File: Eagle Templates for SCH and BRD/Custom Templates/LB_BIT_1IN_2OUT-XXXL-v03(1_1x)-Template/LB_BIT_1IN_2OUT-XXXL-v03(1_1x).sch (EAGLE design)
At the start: 20 parts, among them U1 LV321SOT23-5, U2 LV321SOT23-5, U3 LV321SOT23-5

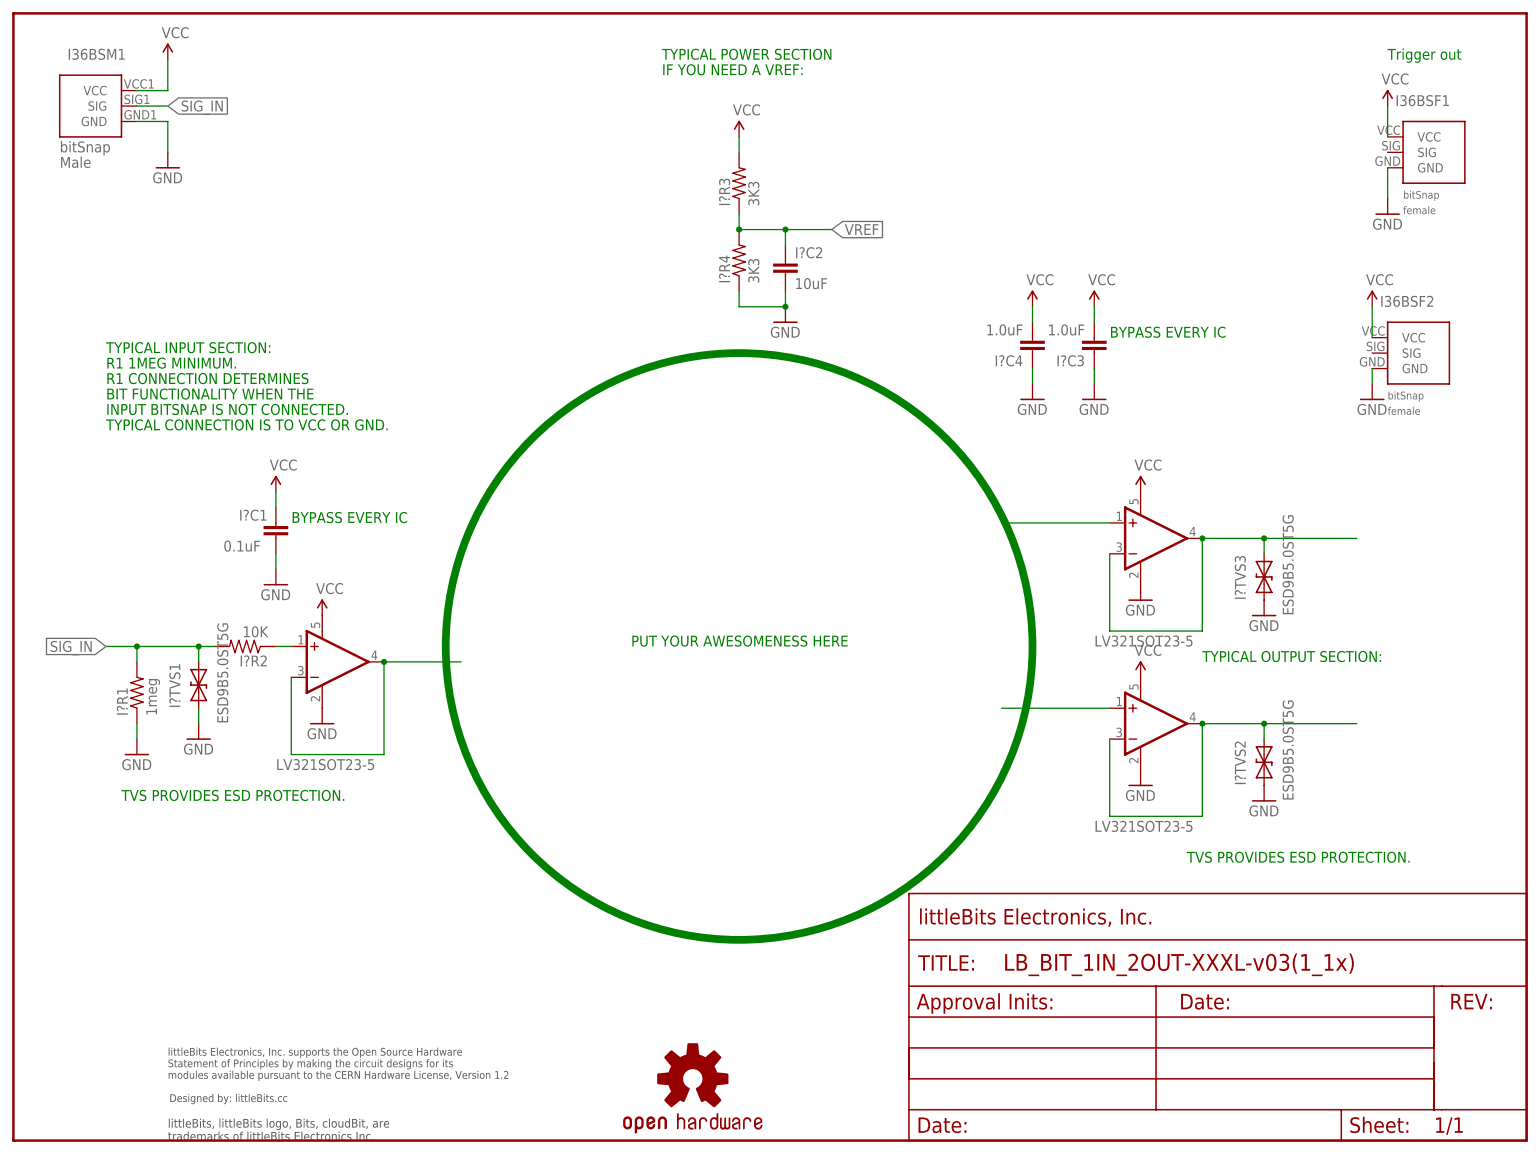
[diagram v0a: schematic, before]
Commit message: Updated templates
- Added ferrite beads
- Moved text and annotations off of Nets layer
- Minor layout changes
- Removed I/O/W prefix from reference designators
- Removed output stage components from output bits
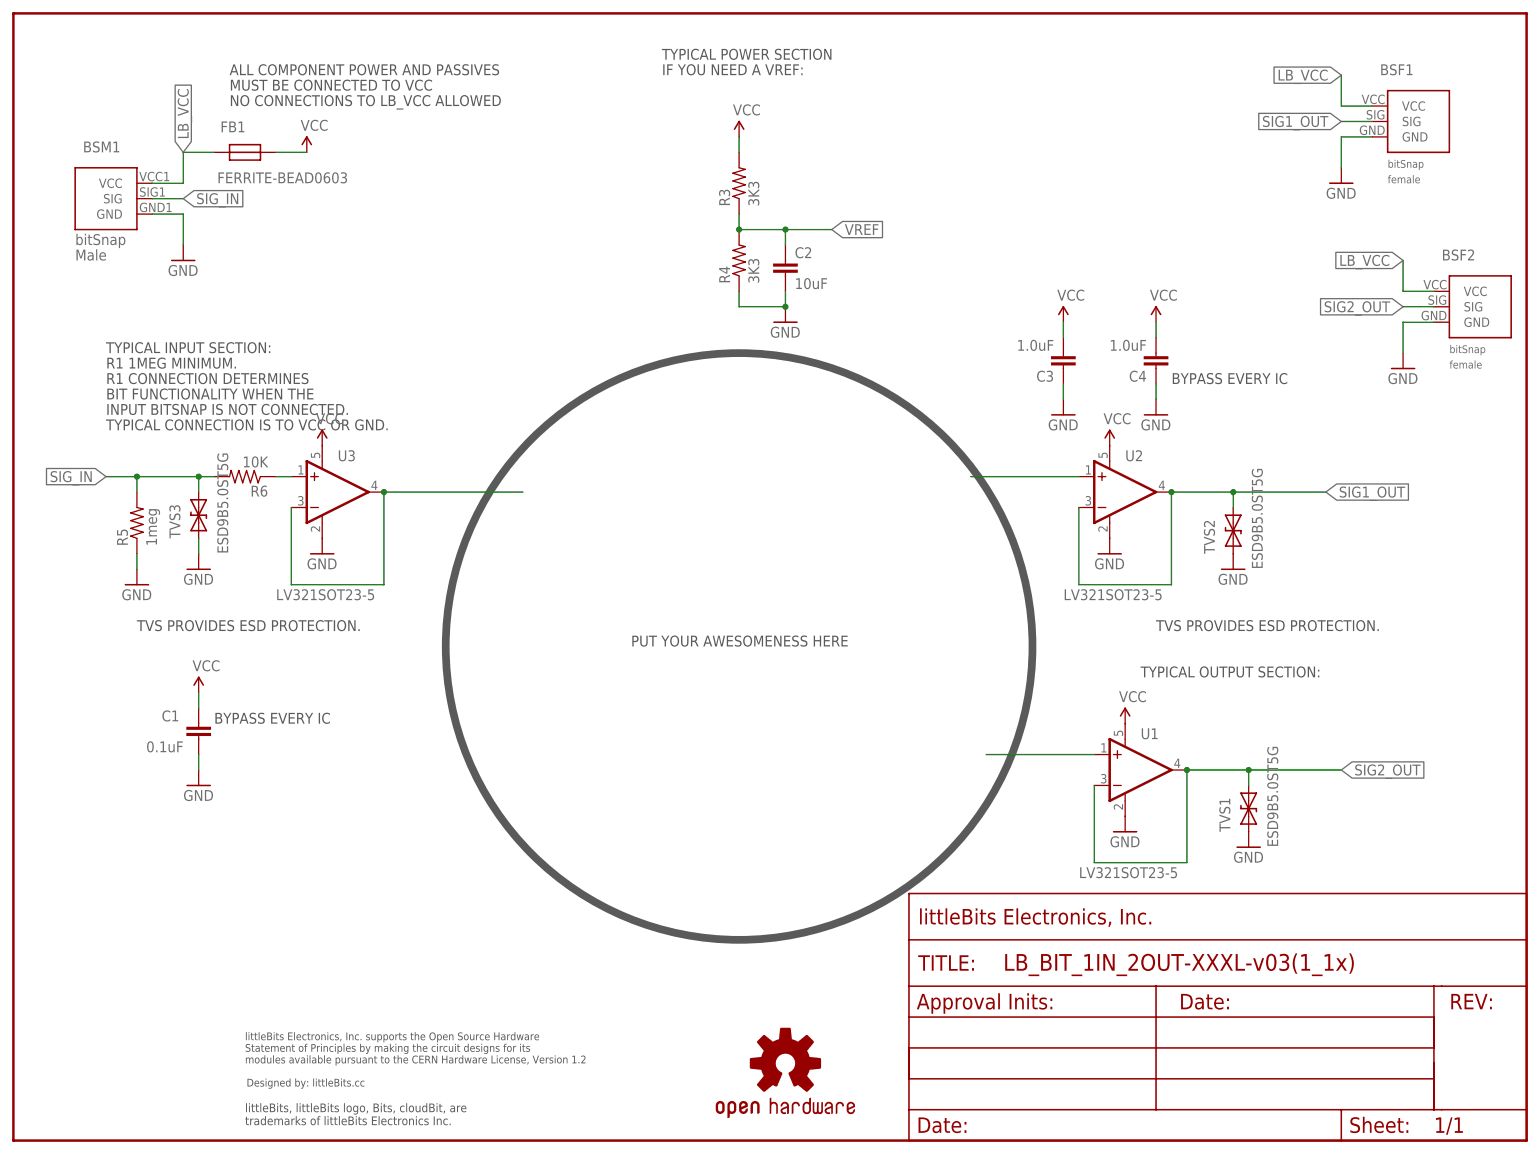
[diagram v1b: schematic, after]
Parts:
- removed I36BSF1, I36BSF2: BITSNAP_V03_FEMALE, bitSnap:BITSNAP_V03_FEMALE
- removed I36BSM1: BITSNAP_V03_MALE, bitSnap:BITSNAP_V03_MALE
- removed I?C1: 0.1uF, LITTLEBITS:CAPCAP-0603
- removed I?C3, I?C4: 1.0uF, LITTLEBITS:CAPCAP-0603
- removed I?R1: 1meg, LITTLEBITS:RESISTOR0603
- removed I?R2: 10K, LITTLEBITS:RESISTOR0603
- removed I?TVS1, I?TVS2, I?TVS3: ESD9B5.0ST5G, LITTLEBITS:DIODE-TVSSOD-923
- removed U$3: OSHWCREDIT, LITTLEBITS:OSHWCREDIT
- added BSF1, BSF2: BITSNAP_V03_FEMALE, bitSnap:BITSNAP_V03_FEMALE
- added BSM1: BITSNAP_V03_MALE, bitSnap:BITSNAP_V03_MALE
- added C1: 0.1uF, LITTLEBITS:CAPCAP-0603
- added C3, C4: 1.0uF, LITTLEBITS:CAPCAP-0603
- added FB1: FERRITE-BEAD0603, LITTLEBITS:FERRITE-BEAD0603
- added R5: 1meg, LITTLEBITS:RESISTOR0603
- added R6: 10K, LITTLEBITS:RESISTOR0603
- added TVS1, TVS2, TVS3: ESD9B5.0ST5G, LITTLEBITS:DIODE-TVSSOD-923
- added U$2: OSHWCREDIT, LITTLEBITS:OSHWCREDIT
- renumbered I?C2 to C2, I?R3 to R3, I?R4 to R4
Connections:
- removed net N$4: I?R2.1, U1.+IN
- removed net SIG_OUT: I?TVS2.C, U2.-IN, U2.OUT
- removed net SIG_OUT1: I?TVS3.C, U3.-IN, U3.OUT
- new net LB_VCC: BSF1.VCC, BSF2.VCC, BSM1.VCC, FB1.P$2
- new net N$5: R6.1, U3.+IN
- new net SIG1_OUT: BSF1.SIG, TVS2.C, U2.-IN, U2.OUT
- new net SIG2_OUT: BSF2.SIG, TVS1.C, U1.-IN, U1.OUT
- net GND: now also BSF1.GND, BSF2.GND, BSM1.GND, C1.2, C3.1, C4.1, R5.1, TVS1.A, TVS2.A, TVS3.A; no longer I36BSF1.GND, I36BSF2.GND, I36BSM1.GND, I?C1.2, I?C3.1, I?C4.1, I?R1.1, I?TVS1.A, I?TVS2.A, I?TVS3.A
- net N$1: now also U3.-IN, U3.OUT; no longer U3.+IN
- net N$2: now also U1.+IN; no longer U1.-IN, U1.OUT
- net SIG_IN: now also BSM1.SIG, R5.2, R6.2, TVS3.C; no longer I36BSM1.SIG, I?R1.2, I?R2.2, I?TVS1.C
- net VCC: now also C1.1, C3.2, C4.2, FB1.P$1; no longer I36BSF1.VCC, I36BSF2.VCC, I36BSM1.VCC, I?C1.1, I?C3.2, I?C4.2
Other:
- note added: "ALL COMPONENT POWER AND PASSIVES"
- note added: "MUST BE CONNECTED TO VCC"
- note added: "NO CONNECTIONS TO LB_VCC ALLOWED"
- note removed: "Trigger out"
